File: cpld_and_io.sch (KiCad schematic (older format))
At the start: 3 parts, among them U11 5M1270ZT144C5N, U13 IS61LV5128AL-10TLI

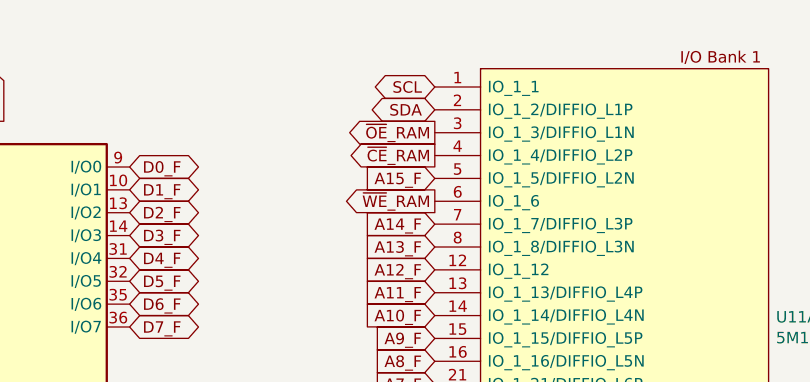
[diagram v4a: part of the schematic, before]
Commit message: recovered layout
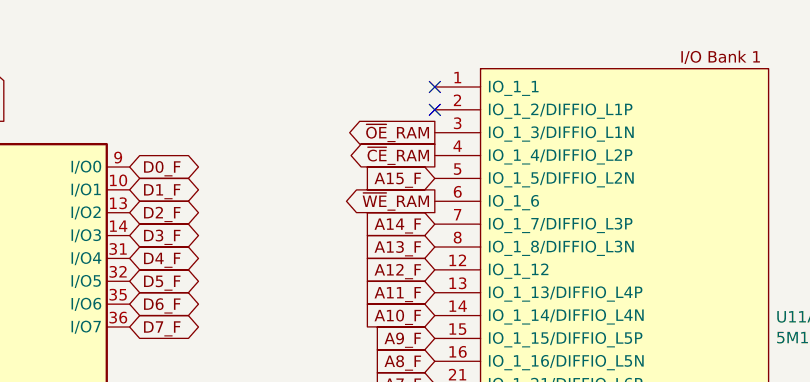
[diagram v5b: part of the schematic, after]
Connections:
- net SCL: no longer names the net of U11.1 (IO_1_1)
- net SDA: no longer names the net of U11.2 (IO_1_2/DIFFIO_L1P)
- no-connect marks 16 -> 18
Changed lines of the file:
@@
 NoConn ~ 1830 2950
 NoConn ~ 1410 2980
-Text GLabel 4365 900  0    50   BiDi ~ 0
-SDA
-Text GLabel 4365 800  0    50   BiDi ~ 0
-SCL
 Text GLabel 6865 1070 0    50   Input ~ 0
 RXB_F
@@
 Wire Wire Line
 	1170 6735 1575 6735
+NoConn ~ 4365 800
+NoConn ~ 4365 900
 $EndSCHEMATC

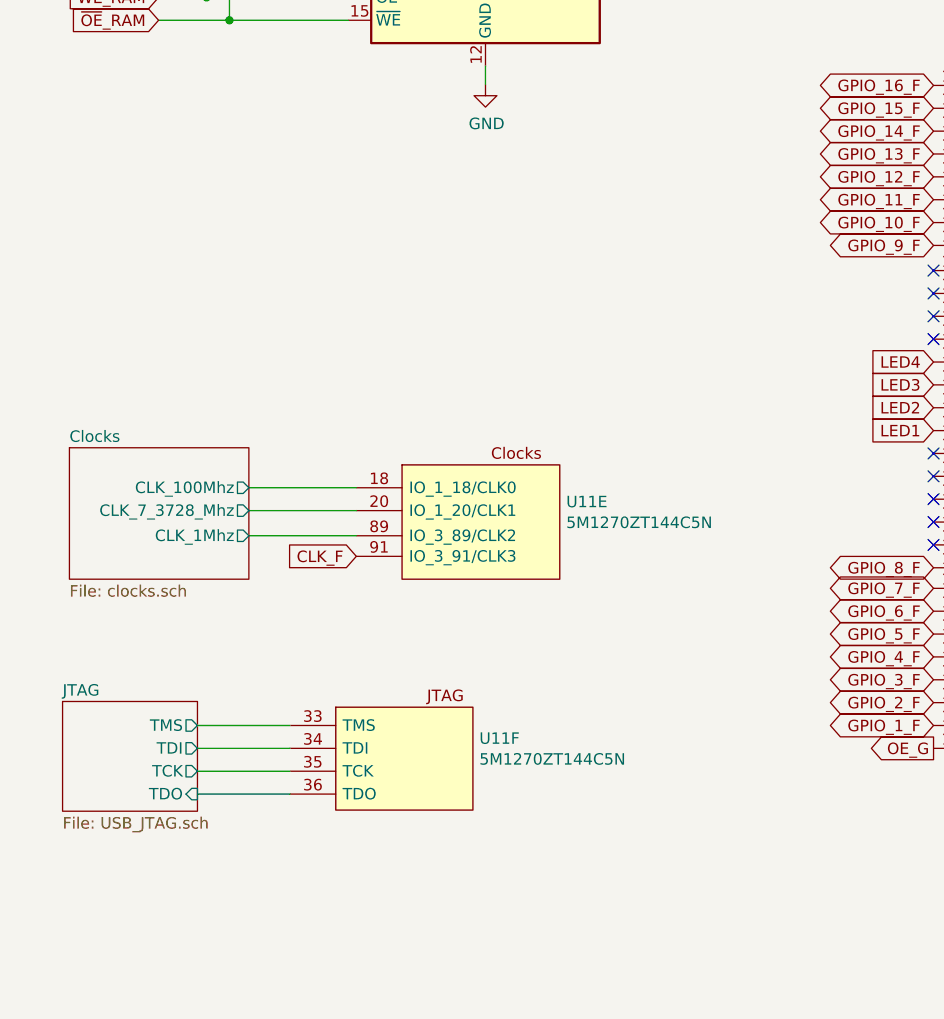
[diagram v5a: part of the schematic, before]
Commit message: placed all parts
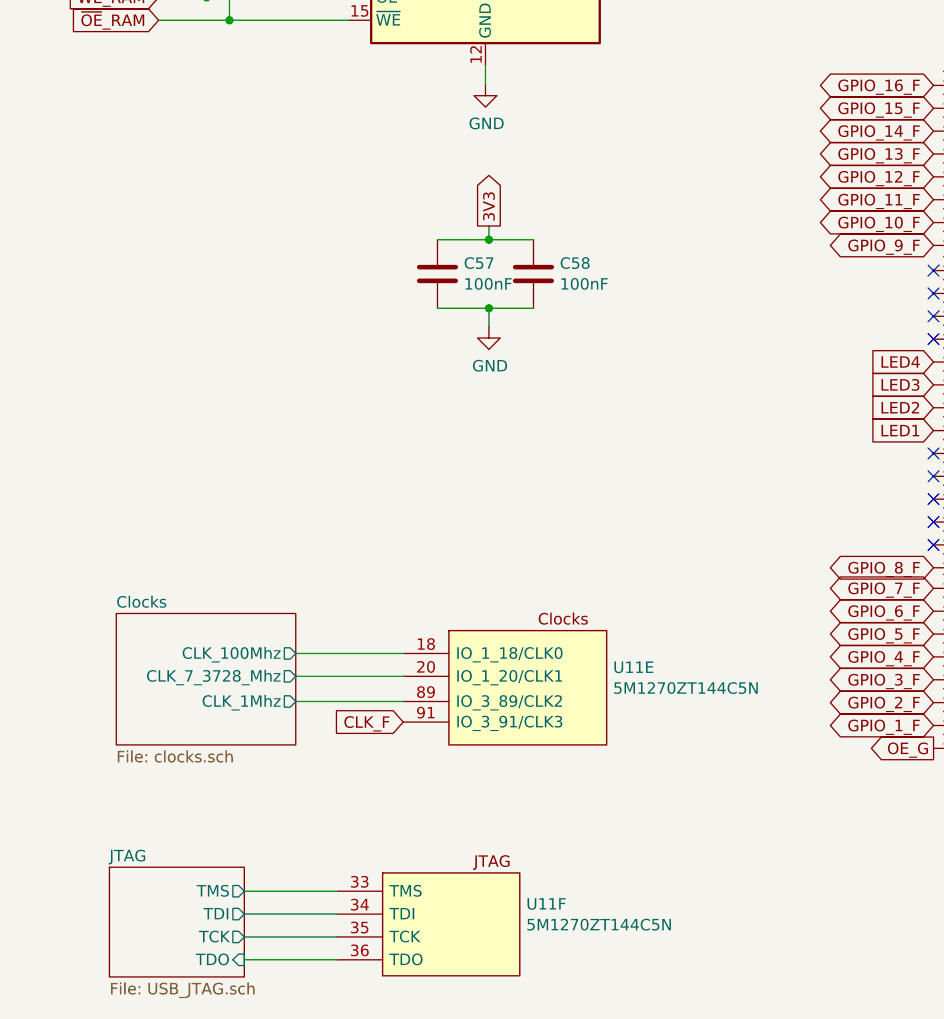
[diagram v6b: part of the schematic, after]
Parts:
- added C57, C58: 100nF, Capacitor_SMD:C_0603_1608Metric_Pad1.05x0.95mm_HandSolder, symbol Device:C
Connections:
- net 3V3: now also C57.1, C58.1
- net GND: now also C57.2, C58.2
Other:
- moved on the sheet: U11E, U11F
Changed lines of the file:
@@
 $EndDescr
 $Sheet
-S 610  5220 785  575
+S 815  5945 785  575
 U 5CFFC458
 F0 "Clocks" 50
 F1 "clocks.sch" 50
-F2 "CLK_100Mhz" O R 1395 5395 50
-F3 "CLK_7_3728_Mhz" O R 1395 5495 50
-F4 "CLK_1Mhz" O R 1395 5605 50
+F2 "CLK_100Mhz" O R 1600 6120 50
+F3 "CLK_7_3728_Mhz" O R 1600 6220 50
+F4 "CLK_1Mhz" O R 1600 6330 50
 $EndSheet
 $Comp
@@
 NoConn ~ 4390 5245
 $Sheet
-S 580  6330 590  480
+S 785  7055 590  480
 U 5D0BF766
 F0 "JTAG" 50
 F1 "USB_JTAG.sch" 50
-F2 "TCK" O R 1170 6635 50
-F3 "TDI" O R 1170 6535 50
-F4 "TDO" I R 1170 6735 50
-F5 "TMS" O R 1170 6435 50
+F2 "TCK" O R 1375 7360 50
+F3 "TDI" O R 1375 7260 50
+F4 "TDO" I R 1375 7460 50
+F5 "TMS" O R 1375 7160 50
 $EndSheet
 $Comp
 L rc2014_max_v-rescue:5M1270ZT144C5N-CPLD_Altera U?
 U 6 1 5D1673E5
-P 2085 6355
+P 2290 7080
 AR Path="/5D1673E5" Ref="U?"  Part="6"
 AR Path="/5D0F9837/5D1673E5" Ref="U?"  Part="6"
 AR Path="/5CFABACD/5D0BF766/5D1673E5" Ref="U?"  Part="6"
 AR Path="/5CFABACD/5D1673E5" Ref="U11"  Part="6"
-F 0 "U11" H 2403 6218 50  0000 L CNN
-F 1 "5M1270ZT144C5N" H 2403 6127 50  0000 L CNN
-F 2 "Package_QFP:TQFP-144_20x20mm_P0.5mm" H 3925 9255 50  0001 L CNN
-F 3 "https://www.mouser.com/datasheet/2/612/max5_handbook-1098935.pdf" H 3925 9155 50  0001 L CNN
-F 4 "CPLD - Complex Programmable Logic Devices CPLD - MAX V 980 Macro 114 IOs" H 3925 9055 50  0001 L CNN "Description"
-F 5 "1.55" H 3925 8955 50  0001 L CNN "Height"
-F 6 "Intel" H 2085 6355 50  0001 C CNN "MFR"
-F 7 "5M1270ZT144C5N" H 2085 6355 50  0001 C CNN "MPN"
-F 8 "5M1270ZT144C5N" H 3925 8555 50  0001 L CNN "Manufacturer_Part_Number"
-F 9 "989-5M1270ZT144C5N" H 2403 6318 50  0001 C CNN "SPN"
-F 10 "Mouser" H 2085 6355 50  0001 C CNN "SPR"
-F 11 "https://www.mouser.com/ProductDetail/989-5M1270ZT144C5N" H 2403 6318 50  0001 C CNN "SPURL"
-	6    2085 6355
+F 0 "U11" H 2608 6943 50  0000 L CNN
+F 1 "5M1270ZT144C5N" H 2608 6852 50  0000 L CNN
+F 2 "Package_QFP:TQFP-144_20x20mm_P0.5mm" H 4130 9980 50  0001 L CNN
+F 3 "https://www.mouser.com/datasheet/2/612/max5_handbook-1098935.pdf" H 4130 9880 50  0001 L CNN
+F 4 "CPLD - Complex Programmable Logic Devices CPLD - MAX V 980 Macro 114 IOs" H 4130 9780 50  0001 L CNN "Description"
+F 5 "1.55" H 4130 9680 50  0001 L CNN "Height"
+F 6 "Intel" H 2290 7080 50  0001 C CNN "MFR"
+F 7 "5M1270ZT144C5N" H 2290 7080 50  0001 C CNN "MPN"
+F 8 "5M1270ZT144C5N" H 4130 9280 50  0001 L CNN "Manufacturer_Part_Number"
+F 9 "989-5M1270ZT144C5N" H 2608 7043 50  0001 C CNN "SPN"
+F 10 "Mouser" H 2290 7080 50  0001 C CNN "SPR"
+F 11 "https://www.mouser.com/ProductDetail/989-5M1270ZT144C5N" H 2608 7043 50  0001 C CNN "SPURL"
+	6    2290 7080
 	1    0    0    -1
 $EndComp
@@
 L rc2014_max_v-rescue:5M1270ZT144C5N-CPLD_Altera U?
 U 5 1 5D1C4FEB
-P 2425 5295
+P 2630 6020
 AR Path="/5D0F9837/5D1C4FEB" Ref="U?"  Part="5"
 AR Path="/5CFABACD/5D1C4FEB" Ref="U11"  Part="5"
 AR Path="/5CFABACD/5CFFC458/5D1C4FEB" Ref="U?"  Part="5"
 AR Path="/5D1C4FEB" Ref="U?"  Part="5"
-F 0 "U11" H 2783 5133 50  0000 L CNN
-F 1 "5M1270ZT144C5N" H 2783 5042 50  0000 L CNN
-F 2 "Package_QFP:TQFP-144_20x20mm_P0.5mm" H 4265 8195 50  0001 L CNN
-F 3 "https://www.mouser.com/datasheet/2/612/max5_handbook-1098935.pdf" H 4265 8095 50  0001 L CNN
-F 4 "CPLD - Complex Programmable Logic Devices CPLD - MAX V 980 Macro 114 IOs" H 4265 7995 50  0001 L CNN "Description"
-F 5 "1.55" H 4265 7895 50  0001 L CNN "Height"
-F 6 "Intel" H 2425 5295 50  0001 C CNN "MFR"
-F 7 "5M1270ZT144C5N" H 2425 5295 50  0001 C CNN "MPN"
-F 8 "5M1270ZT144C5N" H 4265 7495 50  0001 L CNN "Manufacturer_Part_Number"
-F 9 "989-5M1270ZT144C5N" H 2783 5233 50  0001 C CNN "SPN"
-F 10 "Mouser" H 2425 5295 50  0001 C CNN "SPR"
-F 11 "https://www.mouser.com/ProductDetail/989-5M1270ZT144C5N" H 2783 5233 50  0001 C CNN "SPURL"
-	5    2425 5295
-	1    0    0    -1
-$EndComp
-Text GLabel 1865 5695 0    50   Input ~ 0
+F 0 "U11" H 2988 5858 50  0000 L CNN
+F 1 "5M1270ZT144C5N" H 2988 5767 50  0000 L CNN
+F 2 "Package_QFP:TQFP-144_20x20mm_P0.5mm" H 4470 8920 50  0001 L CNN
+F 3 "https://www.mouser.com/datasheet/2/612/max5_handbook-1098935.pdf" H 4470 8820 50  0001 L CNN
+F 4 "CPLD - Complex Programmable Logic Devices CPLD - MAX V 980 Macro 114 IOs" H 4470 8720 50  0001 L CNN "Description"
+F 5 "1.55" H 4470 8620 50  0001 L CNN "Height"
+F 6 "Intel" H 2630 6020 50  0001 C CNN "MFR"
+F 7 "5M1270ZT144C5N" H 2630 6020 50  0001 C CNN "MPN"
+F 8 "5M1270ZT144C5N" H 4470 8220 50  0001 L CNN "Manufacturer_Part_Number"
+F 9 "989-5M1270ZT144C5N" H 2988 5958 50  0001 C CNN "SPN"
+F 10 "Mouser" H 2630 6020 50  0001 C CNN "SPR"
+F 11 "https://www.mouser.com/ProductDetail/989-5M1270ZT144C5N" H 2988 5958 50  0001 C CNN "SPURL"
+	5    2630 6020
+	1    0    0    -1
+$EndComp
+Text GLabel 2070 6420 0    50   Input ~ 0
 CLK_F
 $Sheet
@@
 $EndSheet
 Wire Wire Line
-	1395 5605 1865 5605
-Wire Wire Line
-	1395 5495 1865 5495
-Wire Wire Line
-	1395 5395 1865 5395
-Wire Wire Line
-	1170 6435 1575 6435
-Wire Wire Line
-	1170 6535 1575 6535
-Wire Wire Line
-	1170 6635 1575 6635
-Wire Wire Line
-	1170 6735 1575 6735
+	1600 6330 2070 6330
+Wire Wire Line
+	1600 6220 2070 6220
+Wire Wire Line
+	1600 6120 2070 6120
+Wire Wire Line
+	1375 7160 1780 7160
+Wire Wire Line
+	1375 7260 1780 7260
+Wire Wire Line
+	1375 7360 1780 7360
+Wire Wire Line
+	1375 7460 1780 7460
 NoConn ~ 4365 800
 NoConn ~ 4365 900
+$Comp
+L power:GND #PWR?
+U 1 1 5D12D18F
+P 2445 4690
+AR Path="/5D12D18F" Ref="#PWR?"  Part="1"
+AR Path="/5CB63856/5D12D18F" Ref="#PWR?"  Part="1"
+AR Path="/5CB5AB00/5CB63856/5D12D18F" Ref="#PWR?"  Part="1"
+AR Path="/5CFABACD/5D12D18F" Ref="#PWR029"  Part="1"
+AR Path="/5D2A5E4A/5D12D18F" Ref="#PWR?"  Part="1"
+AR Path="/5CFABACD/5D2103A8/5D12D18F" Ref="#PWR?"  Part="1"
+F 0 "#PWR029" H 2445 4440 50  0001 C CNN
+F 1 "GND" H 2450 4517 50  0000 C CNN
+F 2 "" H 2445 4690 50  0001 C CNN
+F 3 "" H 2445 4690 50  0001 C CNN
+	1    2445 4690
+	1    0    0    -1
+$EndComp
+$Comp
+L Device:C C58
+U 1 1 5D12D19B
+P 2640 4460
+AR Path="/5CFABACD/5D12D19B" Ref="C58"  Part="1"
+AR Path="/5D12D19B" Ref="C?"  Part="1"
+AR Path="/5D2A5E4A/5D12D19B" Ref="C?"  Part="1"
+AR Path="/5CFABACD/5D2103A8/5D12D19B" Ref="C?"  Part="1"
+F 0 "C58" H 2755 4506 50  0000 L CNN
+F 1 "100nF" H 2755 4415 50  0000 L CNN
+F 2 "Capacitor_SMD:C_0603_1608Metric_Pad1.05x0.95mm_HandSolder" H 2678 4310 50  0001 C CNN
+F 3 "https://www.mouser.com/datasheet/2/396/mlcc02_e-1307760.pdf" H 2640 4460 50  0001 C CNN
+F 4 "Multilayer Ceramic Capacitors MLCC - SMD/SMT 0.1uF 25V X5R +/-10% 0603 Gen Purp" H 2755 4606 50  0001 C CNN "Description"
+F 5 "Taiyo Yuden" H -2660 -2240 50  0001 C CNN "MFR"
+F 6 "TMK107BJ104KA-T" H -2660 -2240 50  0001 C CNN "MPN"
+F 7 "963-TMK107BJ104KA-T" H 2755 4606 50  0001 C CNN "SPN"
+F 8 "Mouser" H -2660 -2240 50  0001 C CNN "SPR"
+F 9 "https://www.mouser.com/ProductDetail/963-TMK107BJ104KA-T" H -2660 -2240 50  0001 C CNN "SPURL"
+	1    2640 4460
+	1    0    0    -1
+$EndComp
+$Comp
+L Device:C C57
+U 1 1 5D12D1A7
+P 2220 4460
+AR Path="/5CFABACD/5D12D1A7" Ref="C57"  Part="1"
+AR Path="/5D12D1A7" Ref="C?"  Part="1"
+AR Path="/5D2A5E4A/5D12D1A7" Ref="C?"  Part="1"
+AR Path="/5CFABACD/5D2103A8/5D12D1A7" Ref="C?"  Part="1"
+F 0 "C57" H 2335 4506 50  0000 L CNN
+F 1 "100nF" H 2335 4415 50  0000 L CNN
+F 2 "Capacitor_SMD:C_0603_1608Metric_Pad1.05x0.95mm_HandSolder" H 2258 4310 50  0001 C CNN
+F 3 "https://www.mouser.com/datasheet/2/396/mlcc02_e-1307760.pdf" H 2220 4460 50  0001 C CNN
+F 4 "Multilayer Ceramic Capacitors MLCC - SMD/SMT 0.1uF 25V X5R +/-10% 0603 Gen Purp" H 2335 4606 50  0001 C CNN "Description"
+F 5 "Taiyo Yuden" H -3080 -2240 50  0001 C CNN "MFR"
+F 6 "TMK107BJ104KA-T" H -3080 -2240 50  0001 C CNN "MPN"
+F 7 "963-TMK107BJ104KA-T" H 2335 4606 50  0001 C CNN "SPN"
+F 8 "Mouser" H -3080 -2240 50  0001 C CNN "SPR"
+F 9 "https://www.mouser.com/ProductDetail/963-TMK107BJ104KA-T" H -3080 -2240 50  0001 C CNN "SPURL"
+	1    2220 4460
+	1    0    0    -1
+$EndComp
+Text GLabel 2445 4250 1    50   Output ~ 0
+3V3
+Wire Wire Line
+	2445 4310 2445 4250
+Wire Wire Line
+	2445 4610 2445 4690
+Wire Wire Line
+	2220 4610 2445 4610
+Wire Wire Line
+	2220 4310 2445 4310
+Connection ~ 2445 4310
+Wire Wire Line
+	2445 4310 2640 4310
+Connection ~ 2445 4610
+Wire Wire Line
+	2445 4610 2640 4610
 $EndSCHEMATC

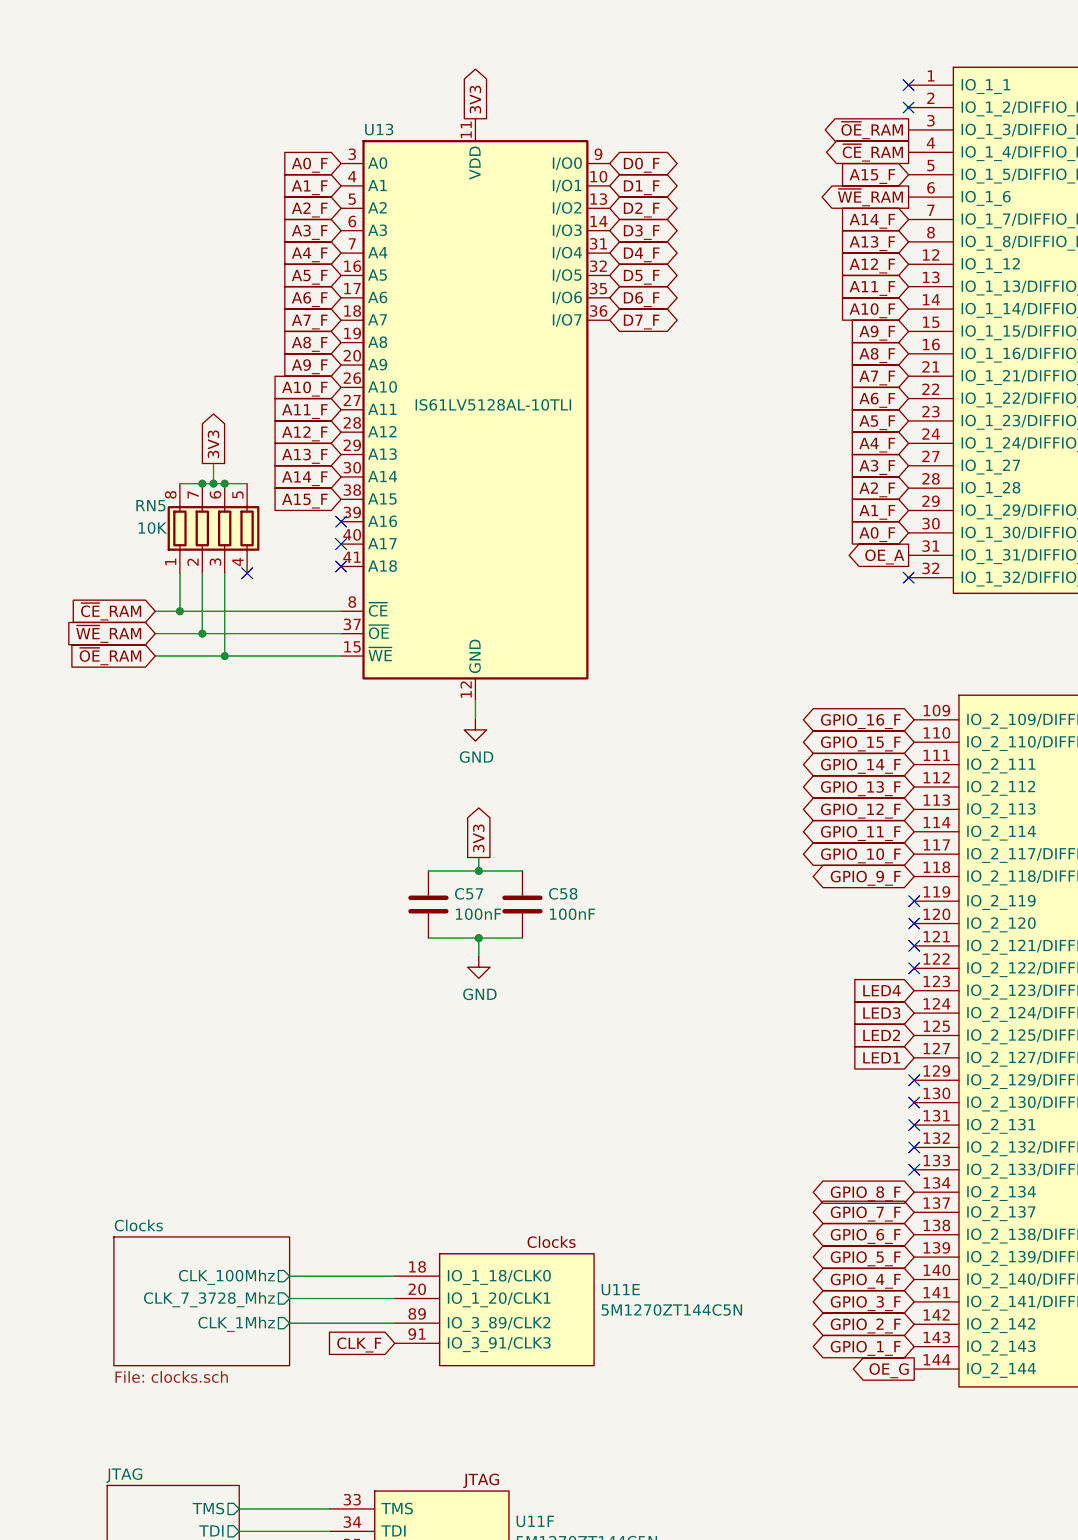
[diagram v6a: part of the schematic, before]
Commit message: Added bus structure, additional pins added, 5V load balancer
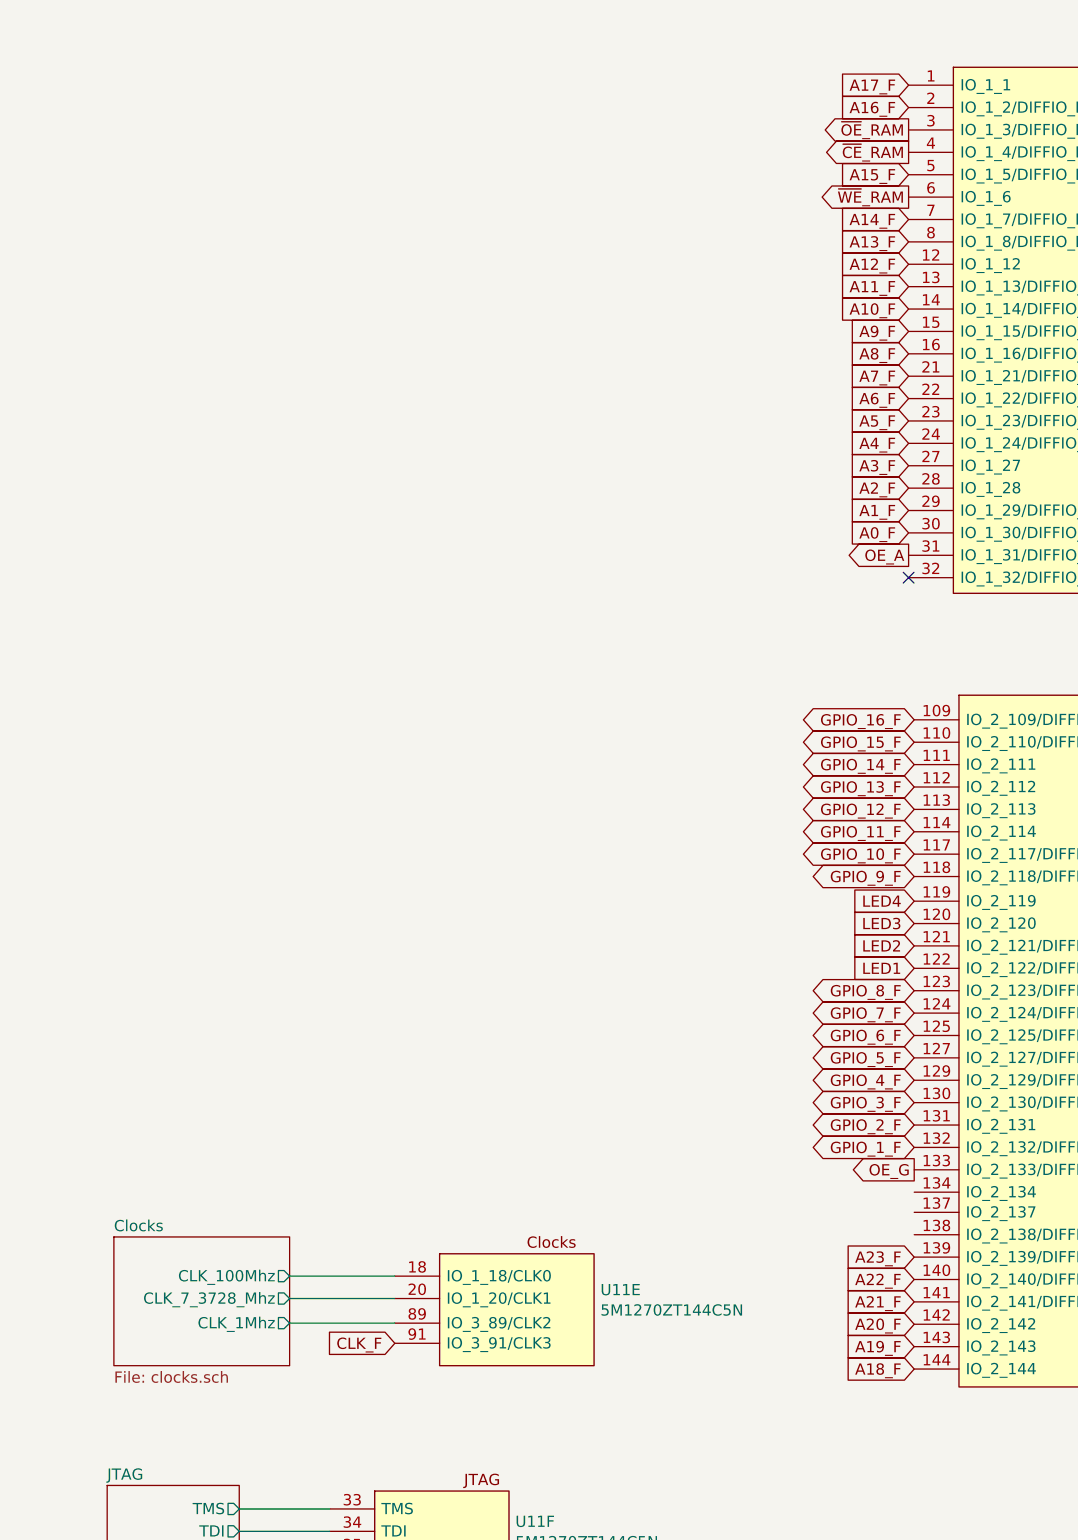
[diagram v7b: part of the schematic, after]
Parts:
- removed C57, C58: 100nF, Capacitor_SMD:C_0603_1608Metric_Pad1.05x0.95mm_HandSolder, symbol Device:C
- removed RN5: 10K, Resistor_SMD:R_Array_Concave_4x0603, symbol Device:R_Pack04
- removed U13: IS61LV5128AL-10TLI, Package_SO:TSOP-II-44_10.16x18.41mm_P0.8mm, symbol rc2014_max_v-rescue:IS61LV5128AL-10TLI-Memory_RAM
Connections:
- net GPIO_1_F: now also U11.132 (IO_2_132/DIFFIO_T3N); no longer U11.143 (IO_2_143)
- net GPIO_2_F: now also U11.131 (IO_2_131); no longer U11.142 (IO_2_142)
- net GPIO_3_F: now also U11.130 (IO_2_130/DIFFIO_T4P); no longer U11.141 (IO_2_141/DIFFIO_T1P)
- net GPIO_4_F: now also U11.129 (IO_2_129/DIFFIO_T4N); no longer U11.140 (IO_2_140/DIFFIO_T1N)
- net GPIO_5_F: now also U11.127 (IO_2_127/DIFFIO_T5P); no longer U11.139 (IO_2_139/DIFFIO_T2P)
- net GPIO_6_F: now also U11.125 (IO_2_125/DIFFIO_T5N); no longer U11.138 (IO_2_138/DIFFIO_T2N)
- net GPIO_7_F: now also U11.124 (IO_2_124/DIFFIO_T6P); no longer U11.137 (IO_2_137)
- net GPIO_8_F: now also U11.123 (IO_2_123/DIFFIO_T6N); no longer U11.134 (IO_2_134)
- net LED1: now also U11.122 (IO_2_122/DIFFIO_T7P); no longer U11.127 (IO_2_127/DIFFIO_T5P)
- net LED2: now also U11.121 (IO_2_121/DIFFIO_T7N); no longer U11.125 (IO_2_125/DIFFIO_T5N)
- net LED3: now also U11.120 (IO_2_120); no longer U11.124 (IO_2_124/DIFFIO_T6P)
- net LED4: now also U11.119 (IO_2_119); no longer U11.123 (IO_2_123/DIFFIO_T6N)
- net OE_G: now also U11.133 (IO_2_133/DIFFIO_T3P); no longer U11.144 (IO_2_144)
- net A17_F: now reaches U11.1 (IO_1_1)
- net A16_F: now reaches U11.2 (IO_1_2/DIFFIO_L1P)
- new net A18_F: U11.144 (IO_2_144)
- new net A19_F: U11.143 (IO_2_143)
- new net A20_F: U11.142 (IO_2_142)
- new net A21_F: U11.141 (IO_2_141/DIFFIO_T1P)
- new net A22_F: U11.140 (IO_2_140/DIFFIO_T1N)
- new net A23_F: U11.139 (IO_2_139/DIFFIO_T2P)
- no-connect marks 18 -> 3
